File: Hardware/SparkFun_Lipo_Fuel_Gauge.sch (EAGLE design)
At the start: 17 parts, among them U2 MAX1704X

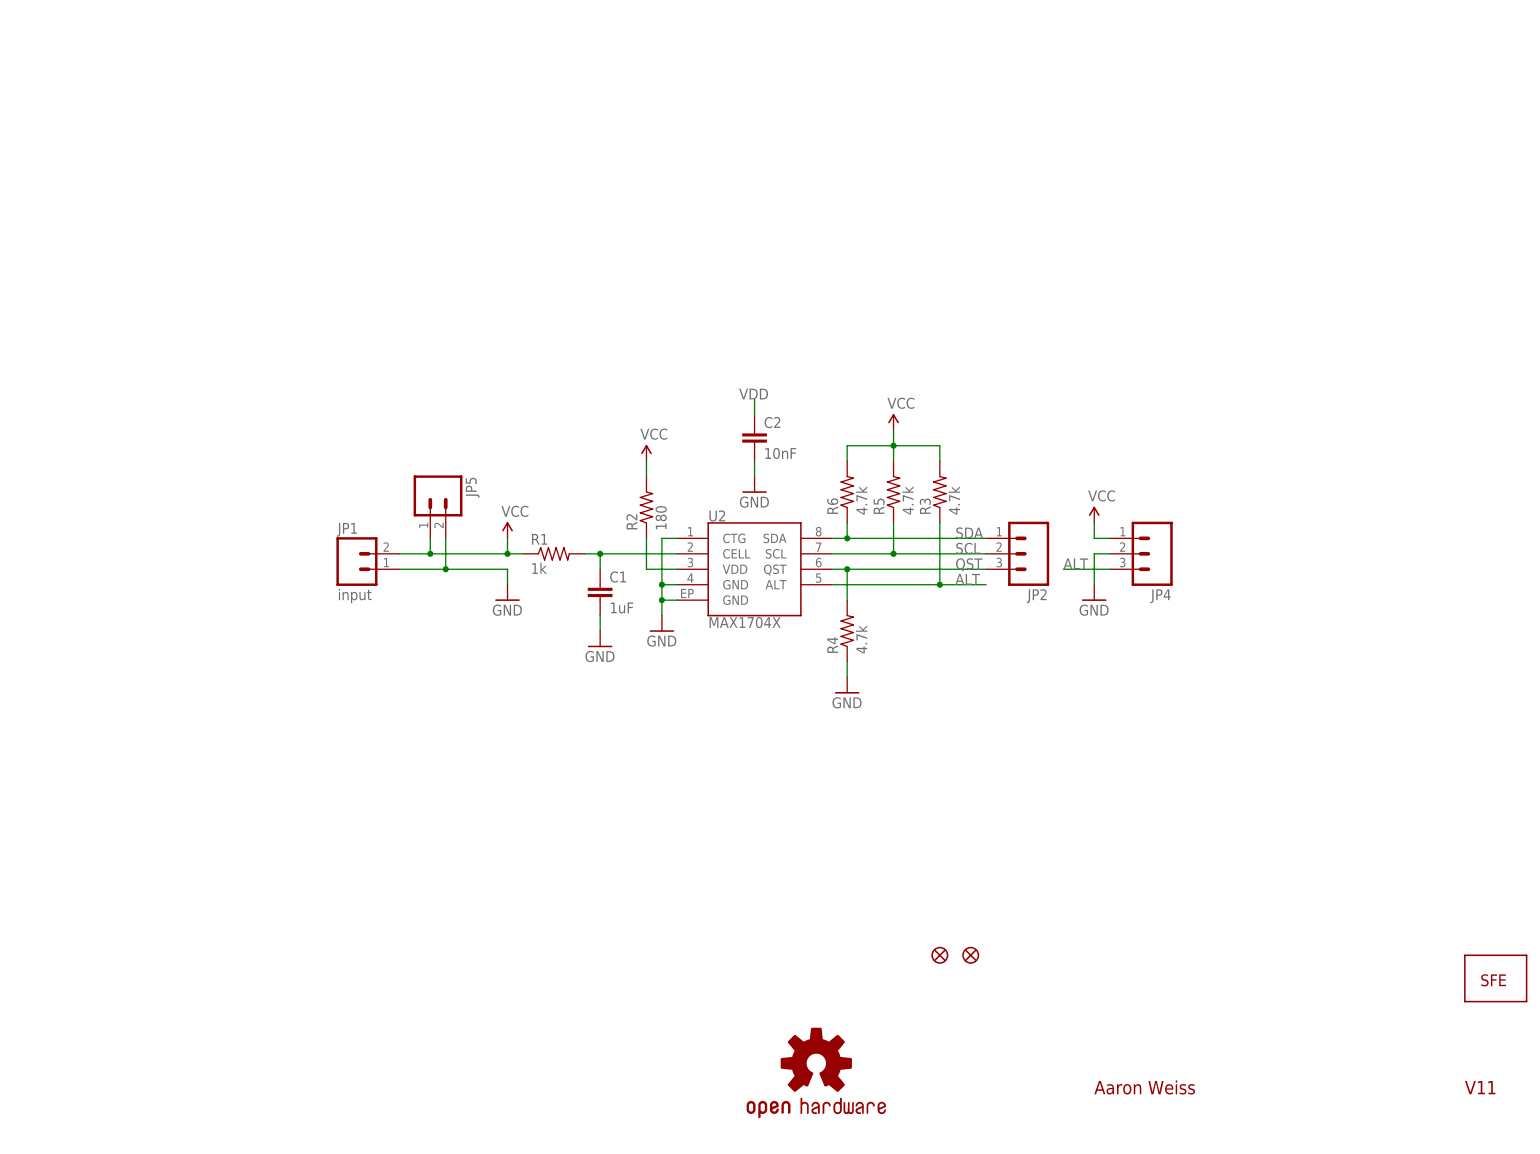
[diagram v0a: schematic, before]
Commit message: Revision updates
Purpose of revision:
VCC connects directly to battery, which means a user could connect a 3V3 signal to 4V2 of the battery, causing things to break (see latest 1-star review on product page). This revision is to separate VCC from V_BATT, allowing users to use any voltage for the logic side. Also update to latest standards while we're at it.

Schematic changes:
Add Revised By
Update revision number
Replace VCC on battery side with V_BATT symbol
Separate regions of circuit
Add dashed lines to distinguish circuit regions
Separate JP1 and JP5
Replace schematic frame with current version
Replace "SFE" symbol with SparkFun logo
Move C2 to connect to VDD directly
Change flags to vector font
Change flags to correct types
Replace fiducials with new version

Board changes:
Add measures
Change copper date to version number
Add battery +/- labels to top silk
Add fiducials to bottom
Decrease GND pour isolation from 12mil to 8mil
Decrease all vias from 20 mil to 15 mil
Approve DRC keepout errors
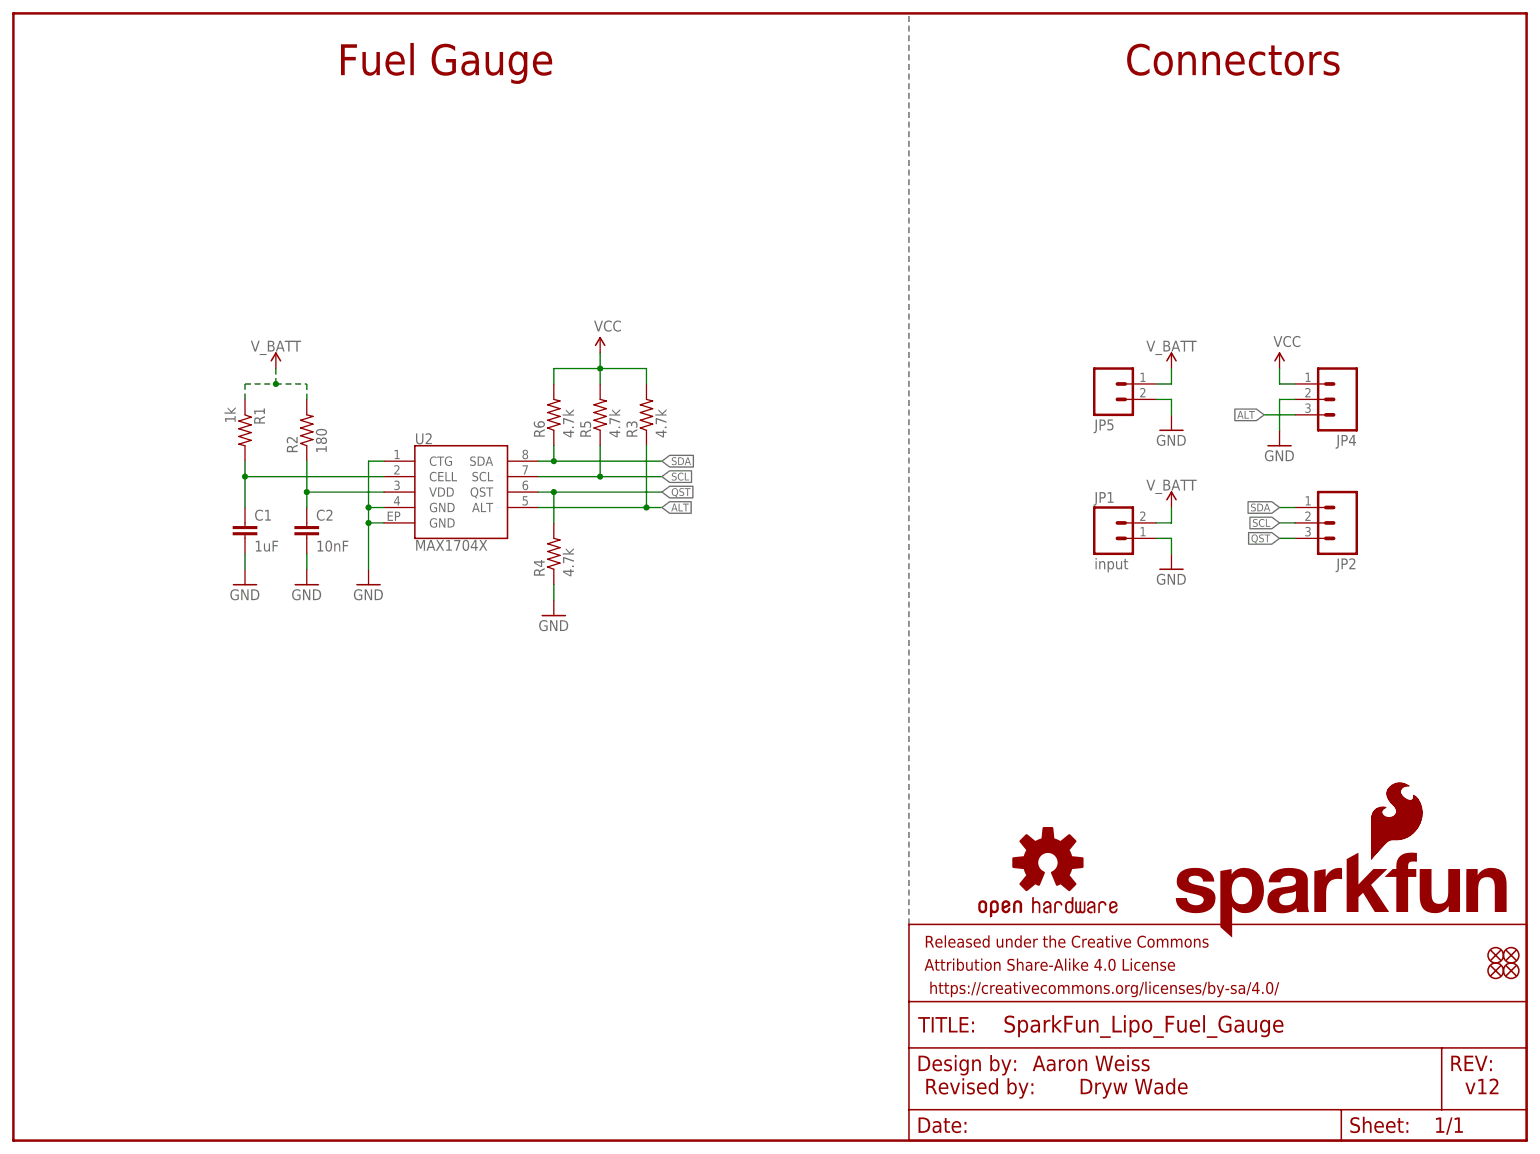
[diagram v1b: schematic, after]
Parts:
- added FRAME1: FRAME-LETTER, SparkFun-Aesthetics:FRAME-LETTER
- added JP8, JP9: FIDUCIALUFIDUCIAL, SparkFun-Aesthetics:FIDUCIALUFIDUCIAL
- added LOGO1: SFE_LOGO_NAME_FLAMEBLANK, SparkFun-Aesthetics:SFE_LOGO_NAME_FLAMEBLANK
- JP3: value LOGO-SFESK -> SFE_LOGO_FLAME.1_INCH; device SparkFun:LOGO-SFESK -> SparkFun-Aesthetics:SFE_LOGO_FLAME.1_INCH
- JP6, JP7: value FIDUCIAL1X2.5 -> FIDUCIALUFIDUCIAL; device abes:FIDUCIAL1X2.5 -> SparkFun-Aesthetics:FIDUCIALUFIDUCIAL
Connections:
- new net V_BATT: JP1.2, JP5.1, R1.1, R2.2
- net VCC: no longer JP1.2, JP5.1, R1.1, R2.2
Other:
- note added: "Connectors"
- note added: "Dryw Wade"
- note added: "Fuel Gauge"
- note added: "Revised by:"
- note added: "v12"
- note removed: "V11"
- moved on the sheet: C1, C2, JP1, JP2, JP4, JP5, R1, R2, R3, R4, R5, R6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

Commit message: Design review updates
Schematic:
Replace old Eagle devices with current ones
Update MAX1704X symbol to match current standards
Add warning about single cell LiPo only
Add voltage range for V_BATT and VCC
Add I2C pullup isolation jumper

Board:
Fix routing with new footprints
Route straight out of all pads
Add vias to increase GND pour
Switch to Buzzard silk labels
Add units to measures
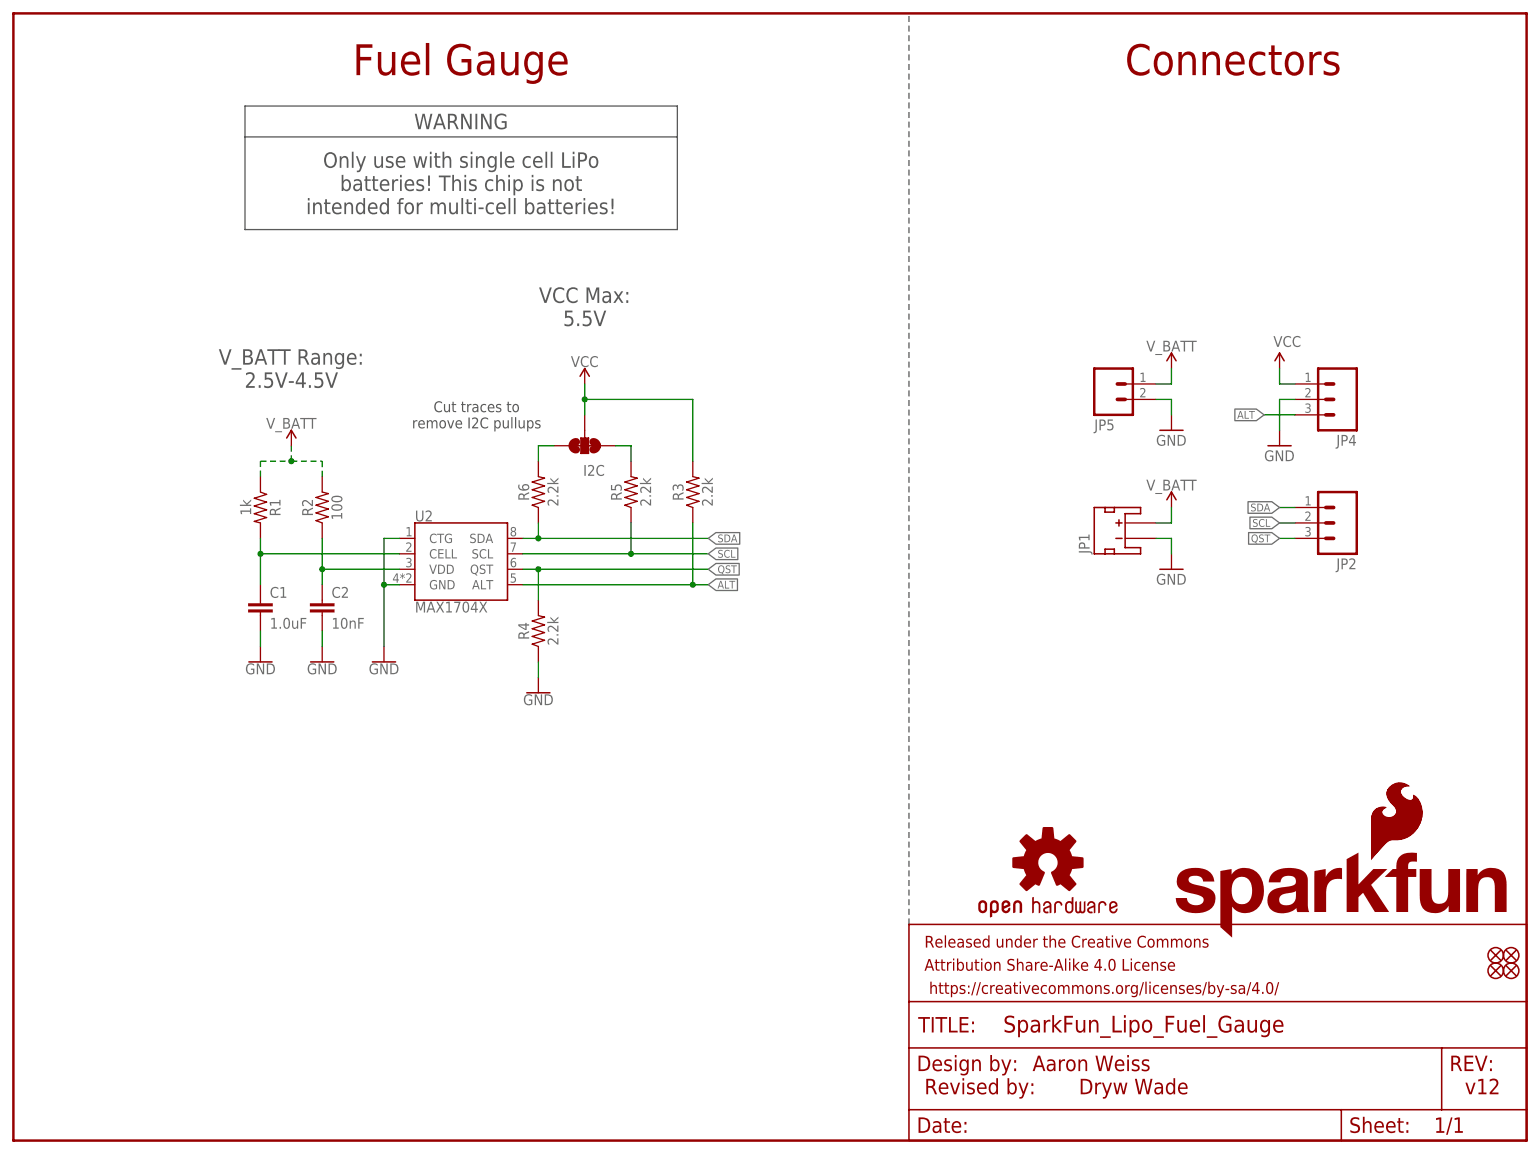
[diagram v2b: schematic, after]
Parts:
- added I2C: JUMPER-SMT_3_2-NC_TRACE_SILK, SparkFun-Jumpers:JUMPER-SMT_3_2-NC_TRACE_SILK
- C1: value 1uF -> 1.0uF; device SparkFun:CAP0402-CAP -> SparkFun-Capacitors:1.0UF-0402T-16V-10%
- C2: device SparkFun:CAP0402-CAP -> SparkFun-Capacitors:10NF-0402T-25V-10%
- JP1: device SparkFun:M02-JST-2MM-SMT -> SparkFun-Connectors:JST_2MM_MALE
- JP2, JP4: device SparkFun:M03PTH -> SparkFun-Connectors:CONN_031X03_NO_SILK
- JP5: device SparkFun:M02PTH -> SparkFun-Connectors:CONN_021X02_NO_SILK
- R1: device SparkFun:RESISTOR0402-RES -> SparkFun-Resistors:1KOHM-0402T-1/16W-1%
- R2: value 180 -> 100; device SparkFun:RESISTOR0402-RES -> SparkFun-Resistors:100OHM-0402-TIGHT-1/16W-1%
- R3, R4, R5, R6: value 4.7k -> 2.2k; device SparkFun:RESISTOR0402-RES -> SparkFun-Resistors:2.2KOHM-0402T-1/16W-1%
- U2: device SparkFun:MAX1704X -> SparkFun-IC-Power:MAX1704X
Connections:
- new net N$1: I2C.3, R6.2
- new net N$3: I2C.1, R5.2
- net GND: now also JP1.-, U2.GND; no longer JP1.1, U2.GND@4, U2.GND@EP
- net VCC: now also I2C.2; no longer R5.2, R6.2
- net V_BATT: now also JP1.+; no longer JP1.2
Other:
- note added: "Cut traces to remove I2C pullups"
- note added: "Only use with single cell LiPo batteries! This chip is not intended for multi-cell batteries!"
- note added: "VCC Max: 5.5V"
- note added: "V_BATT Range: 2.5V-4.5V"
- note added: "WARNING"
- moved on the sheet: C1, C2, R1, R2, R3, R4, R5, R6
